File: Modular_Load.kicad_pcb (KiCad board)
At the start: 2 copper layers, 65 x 40 mm, 61 parts, among them J2 Conn_01x04_Male, J3 7466203, J4 Conn_01x02_Male, J5 7466203, Q2 IGT65R025D2, U1 ADA4807-4

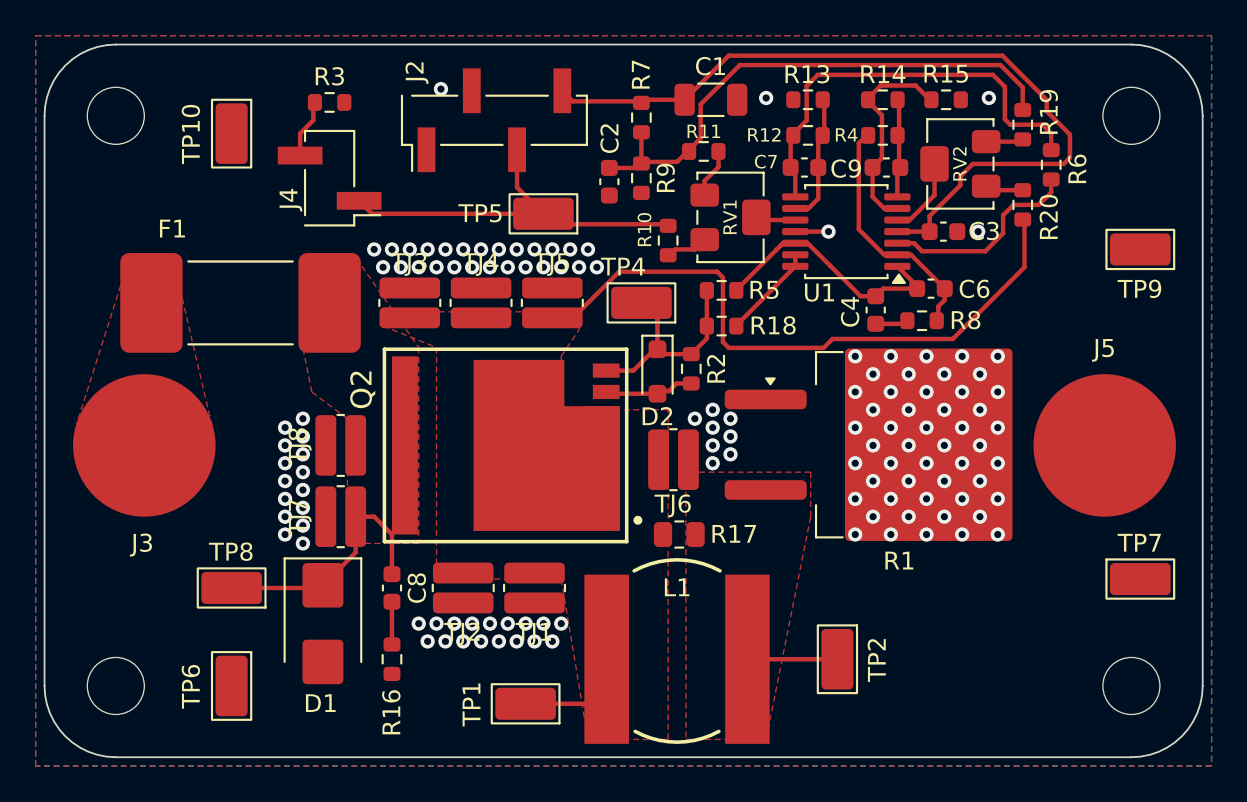
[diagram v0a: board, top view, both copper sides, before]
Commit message: Add files via upload
V2, added MMCX connectors, adjusted gain tuning, changed control connector, thermal layout update.
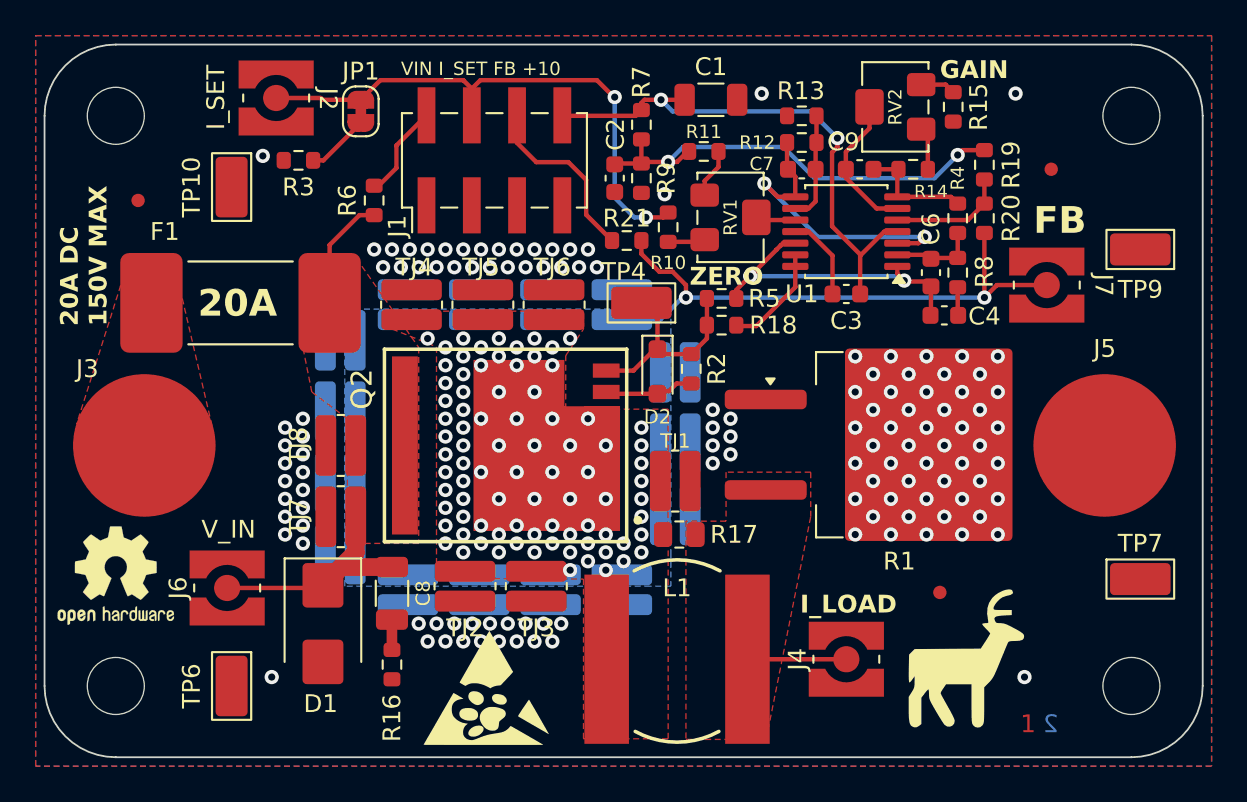
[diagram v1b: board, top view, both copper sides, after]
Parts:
- removed TP1, TP2, TP5, TP8: 5015, TestPoint:TestPoint_Keystone_5015_Micro_Mini
- added FD1: Fiducial_0.75mm_Mask1.5mm, Fiducial:Fiducial_0.75mm_Mask1.5mm, F.Cu at (96.8, 65.8)
- added FD2: Fiducial_0.75mm_Mask1.5mm, Fiducial:Fiducial_0.75mm_Mask1.5mm, F.Cu at (141.8, 87.8)
- added FD3: Fiducial_0.75mm_Mask1.5mm, Fiducial:Fiducial_0.75mm_Mask1.5mm, F.Cu at (148.0, 64.0)
- added G***: LOGO, LOGO, F.Cu at (143.0, 91.5)
- added G***: LOGO, LOGO, F.Cu at (116.5, 93.2)
- added J1: Conn_02x04_Odd_Even, Connector_PinHeader_2.54mm:PinHeader_2x04_P2.54mm_Vertical_SMD, F.Cu at (116.8, 63.5)
- added J6: Conn_Coaxial, Connector_Coaxial:WR-MMCX_Wuerth_66012102111404_Vertical, F.Cu at (101.8, 87.5)
- added J7: Conn_Coaxial, Connector_Coaxial:WR-MMCX_Wuerth_66012102111404_Vertical, F.Cu at (147.8, 70.5)
- added JP1: SolderJumper_2_Bridged, Jumper:SolderJumper-2_P1.3mm_Bridged_RoundedPad1.0x1.5mm, F.Cu at (109.2, 60.8)
- added Layers: LayerMarker_2_3.81x2.54mm_TextH1mm_P1.27mm_BottomMirrored, Symbol:LayerMarker_2_3.81x2.54mm_TextH1mm_P1.27mm_BottomMirrored, F.Cu at (146.7, 96.4)
- added R21: 1Meg, Resistor_SMD:R_0603_1608Metric, F.Cu at (124.2, 68.0)
- added REF**: OSHW-Logo2_7.3x6mm_SilkScreen, Symbol:OSHW-Logo2_7.3x6mm_SilkScreen, F.Cu at (95.5, 86.8)
- added TJ10: THJP0612ABT1, Resistor_SMD:R_0612_1632Metric_Pad1.18x3.40mm_HandSolder, B.Cu at (108.1, 77.6)
- added TJ11: THJP0612ABT1, Resistor_SMD:R_0612_1632Metric_Pad1.18x3.40mm_HandSolder, B.Cu at (108.1, 81.6)
- added TJ12: THJP0612ABT1, Resistor_SMD:R_0612_1632Metric_Pad1.18x3.40mm_HandSolder, B.Cu at (108.1, 85.6)
- added TJ13: THJP0612ABT1, Resistor_SMD:R_0612_1632Metric_Pad1.18x3.40mm_HandSolder, B.Cu at (111.9, 87.6)
- added TJ14: THJP0612ABT1, Resistor_SMD:R_0612_1632Metric_Pad1.18x3.40mm_HandSolder, B.Cu at (115.9, 87.6)
- added TJ15: THJP0612ABT1, Resistor_SMD:R_0612_1632Metric_Pad1.18x3.40mm_HandSolder, B.Cu at (123.9, 71.6)
- added TJ16: THJP0612ABT1, Resistor_SMD:R_0612_1632Metric_Pad1.18x3.40mm_HandSolder, B.Cu at (119.9, 71.6)
- added TJ17: THJP0612ABT1, Resistor_SMD:R_0612_1632Metric_Pad1.18x3.40mm_HandSolder, B.Cu at (115.9, 71.6)
- added TJ18: THJP0612ABT1, Resistor_SMD:R_0612_1632Metric_Pad1.18x3.40mm_HandSolder, B.Cu at (111.9, 71.6)
- added TJ19: THJP0612ABT1, Resistor_SMD:R_0612_1632Metric_Pad1.18x3.40mm_HandSolder, B.Cu at (123.9, 87.6)
- added TJ20: THJP0612ABT1, Resistor_SMD:R_0612_1632Metric_Pad1.18x3.40mm_HandSolder, B.Cu at (119.9, 87.6)
- added TJ21: THJP0612ABT1, Resistor_SMD:R_0612_1632Metric_Pad1.18x3.40mm_HandSolder, B.Cu at (126.9, 75.4)
- added TJ22: THJP0612ABT1, Resistor_SMD:R_0612_1632Metric_Pad1.18x3.40mm_HandSolder, B.Cu at (126.9, 83.4)
- added TJ23: THJP0612ABT1, Resistor_SMD:R_0612_1632Metric_Pad1.18x3.40mm_HandSolder, B.Cu at (126.9, 79.4)
- added TJ9: THJP0612ABT1, Resistor_SMD:R_0612_1632Metric_Pad1.18x3.40mm_HandSolder, B.Cu at (108.1, 73.6)
- C7, C9: value 1p -> 10p
- C8: footprint Capacitor_SMD:C_0603_1608Metric -> Capacitor_SMD:C_1206_3216Metric
- J2: value Conn_01x04_Male -> Conn_Coaxial; footprint Connector_PinHeader_2.54mm:PinHeader_1x04_P2.54mm_Vertical_SMD_Pin1Left -> Connector_Coaxial:WR-MMCX_Wuerth_66012102111404_Vertical
- J4: value Conn_01x02_Male -> Conn_Coaxial; footprint Connector_PinHeader_2.54mm:PinHeader_1x02_P2.54mm_Vertical_SMD_Pin1Left -> Connector_Coaxial:WR-MMCX_Wuerth_66012102111404_Vertical
- R6: value 0 -> 1Meg
- moved J4 39.6 mm to (136.5, 91.5), turned to 90 degrees
- moved R6 38.1 mm to (110.0, 65.8), turned to -90 degrees
- moved TJ3 17.4 mm to (119.1, 87.4), turned to -90 degrees
- moved J2 12.3 mm to (104.5, 60.0)
- moved TJ6 11.0 mm to (120.1, 71.6), turned to 90 degrees
- moved TJ1 9.92 mm to (126.9, 81.5), turned to 0 degrees
- moved C3 6.48 mm to (136.5, 71.0), turned to 180 degrees
- moved R4 6.27 mm to (142.8, 66.8), turned to -90 degrees
- moved RV2 4.85 mm to (139.2, 60.5)
- moved R14 4.25 mm to (140.2, 64.0), turned to 0 degrees
- moved TJ4 3.90 mm to (112.1, 71.6)
- moved TJ5 3.90 mm to (116.1, 71.6)
- moved C4 3.86 mm to (142.0, 72.2), turned to 180 degrees
- moved R3 3.69 mm to (105.8, 63.5), turned to 180 degrees
- moved R8 3.36 mm to (142.8, 69.8), turned to -90 degrees
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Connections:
- C7 pad 1: Net-(C7-Pad1) -> Net-(U1A-+)
- J2 pad 1: unconnected-(J2-Pin_1-Pad1) -> /I_SET
- J4 pad 1: /I_SET -> Net-(J4-In)
- J4 pad 2: Net-(J4-Pin_2) -> GND
- L1 pad 2: Net-(L1-Pad2) -> Net-(J4-In)
- R1 pad 2: Net-(L1-Pad2) -> Net-(J4-In)
- R12 pad 1: Net-(C7-Pad1) -> Net-(U1A-+)
- R14 pad 2: Net-(U1B--) -> Net-(R14-Pad2)
- R15 pad 1: Net-(U1B--) -> Net-(R15-Pad1)
- R17 pad 1: Net-(L1-Pad2) -> Net-(J4-In)
- R19 pad 1: Net-(R19-Pad1) -> Net-(U1B-+)
- R20 pad 2: Net-(R20-Pad2) -> Net-(U1B-+)
- R3 pad 1: Net-(J4-Pin_2) -> Net-(JP1-A)
- R6 pad 1: Net-(U1A-+) -> Net-(J1-Pin_2)
- R6 pad 2: Net-(C7-Pad1) -> Net-(D1-A1)
- RV2 pad 1: Net-(R20-Pad2) -> Net-(R14-Pad2)
- RV2 pad 2: Net-(U1B-+) -> Net-(U1B--)
- RV2 pad 3: Net-(R19-Pad1) -> Net-(R15-Pad1)
- U1 pad 8: Net-(C7-Pad1) -> Net-(U1A-+)
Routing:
- net Net-(C7-Pad1): track 24.1 -> 0.00 mm
- net +10V: track 45.6 -> 30.4 mm, vias 0 -> 2
- net Net-(J1-Pin_6): track 0.00 -> 10.3 mm
- net /FB: track 42.7 -> 33.0 mm, vias 0 -> 86
- net /I_SET: track 22.1 -> 31.0 mm, vias 0 -> 2
- net Net-(U1A--): track 13.6 -> 5.14 mm
- net Net-(D1-A1): track 14.5 -> 20.8 mm
- net Net-(U1A-+): track 11.5 -> 17.2 mm, vias 0 -> 2
- net Net-(J4-In): track 0.00 -> 5.55 mm
- net Net-(J1-Pin_2): track 0.00 -> 5.31 mm
- net Net-(L1-Pad2): track 5.05 -> 0.00 mm
- net /Offset: track 30.2 -> 25.3 mm, vias 0 -> 2
- net Net-(U1B--): track 11.9 -> 8.13 mm
- net Net-(JP1-A): track 0.00 -> 3.54 mm
- net Net-(U1D-+): track 14.3 -> 17.9 mm, vias 0 -> 2
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- added copper zone on B.Cu, net /FB
- added copper zone on F.Cu, net Net-(J4-In)
- removed copper zone on F.Cu, net Net-(L1-Pad2)
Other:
- board text added: "20A"
- board text added: "20A DC 150V MAX"
- board text added: "FB"
- board text added: "GAIN"
- board text added: "I_LOAD"
- board text added: "I_SET"
- board text added: "VIN I_SET FB +10"
- board text added: "V_IN"
- board text added: "ZERO"

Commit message: V3 Update
Thermal improvements, double-sided assembly, better reference stability
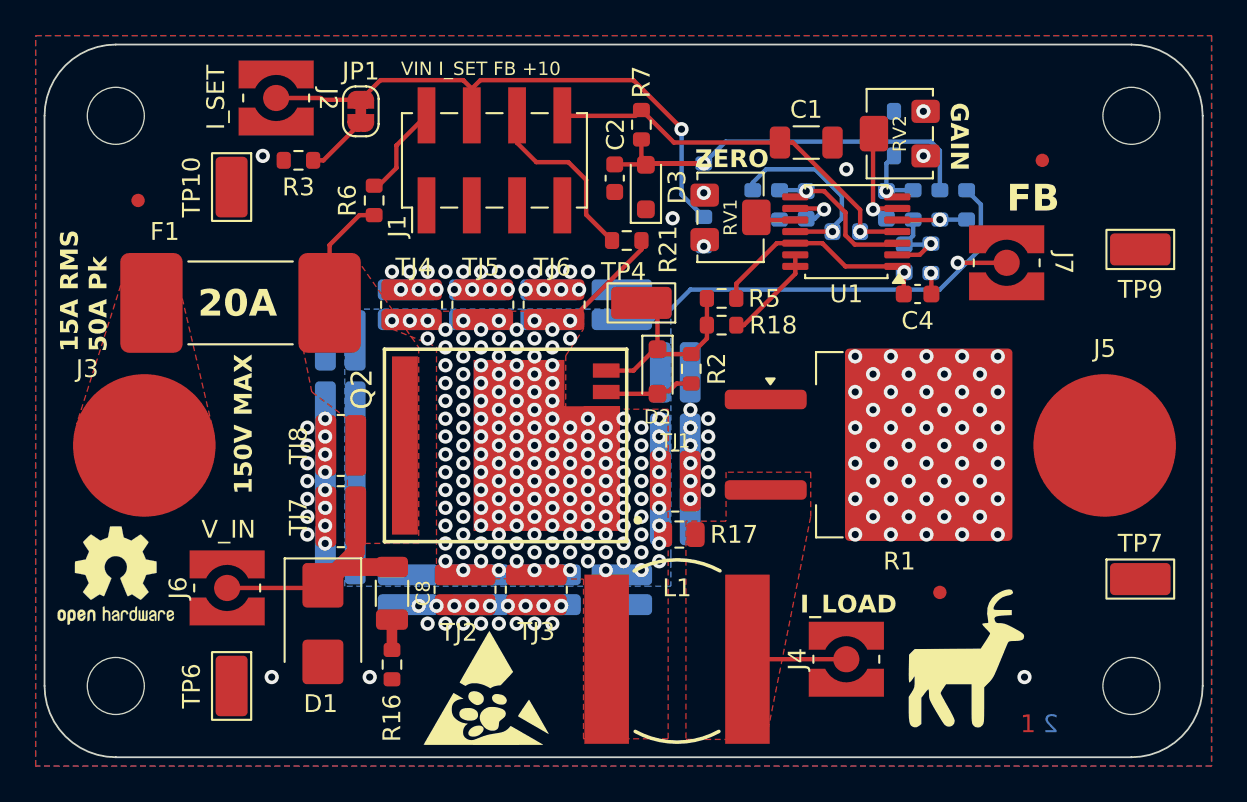
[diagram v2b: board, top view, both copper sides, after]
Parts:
- removed R9: 2k, Resistor_SMD:R_0603_1608Metric
- added D3: 5.6V, Diode_SMD:D_SOD-323_HandSoldering, F.Cu at (125.2, 65.0)
- C3, C6, C7, C9, R10, R11, R12, R13, R14, R15, R19, R20, R4, R8: moved to B.Cu
- moved C1 5.86 mm to (134.2, 62.5)
- moved R13 5.71 mm to (131.2, 66.0), turned to 90 degrees
- moved R12 3.72 mm to (132.8, 66.0), turned to -90 degrees
- moved C3 3.50 mm to (136.5, 67.5)
- moved R19 3.36 mm to (141.8, 66.0)
- moved R4 2.61 mm to (140.2, 66.0)
- moved J7 2.57 mm to (145.5, 69.2)
- moved R15 2.51 mm to (140.0, 60.8), turned to 180 degrees
- moved C9 2.50 mm to (138.8, 66.0), turned to -90 degrees
- moved C7 2.02 mm to (134.2, 66.0), turned to -90 degrees
- moved R10 2.02 mm to (128.5, 67.5)
- moved C4 1.92 mm to (140.5, 71.0)
- moved C6 1.70 mm to (139.8, 69.0)
- moved R8 1.70 mm to (141.2, 69.0)
- moved RV2 1.52 mm to (139.5, 62.0)
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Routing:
- net +10V: track 30.4 -> 22.0 mm, vias 2 -> 1
- net Net-(U1A-+): track 17.2 -> 9.40 mm, vias 2 -> 1
- net GND: track 5.15 -> 11.0 mm, vias 121 -> 123
- net Net-(U1D-+): track 17.9 -> 13.1 mm, vias 2 -> 1
- net Net-(R11-Pad1): track 2.77 -> 0.00 mm, vias 0 -> 1
- net Net-(U1B-+): track 6.62 -> 3.90 mm, vias 0 -> 1
- net Net-(R14-Pad2): track 2.41 -> 0.00 mm, vias 0 -> 1
- net Net-(R10-Pad2): track 2.12 -> 0.00 mm, vias 0 -> 1
- net Net-(C9-Pad1): track 6.52 -> 4.42 mm, vias 0 -> 1
- net Net-(R15-Pad1): track 1.98 -> 0.00 mm, vias 0 -> 1
- net /FB: track 33.0 -> 34.8 mm, vias 86 -> 162
- net Net-(U1B--): track 8.13 -> 6.62 mm, vias 0 -> 1
- net Net-(D2-K): track 11.8 -> 10.6 mm
- net /I_SET: track 31.0 -> 31.8 mm, vias 2 -> 1
- net /Offset: track 25.3 -> 26.0 mm, vias 2 -> 1
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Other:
- board text added: "150V MAX"
- board text added: "15A RMS 50A Pk"
- board text removed: "20A DC 150V MAX"

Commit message: Added heatsink drawings, updated component 3D models
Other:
- board text added: "Copper Coin Artwork"
